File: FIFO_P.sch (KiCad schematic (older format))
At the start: 81 parts, among them J1 Vin, J2 ICLK, J3 Screw_Terminal_01x08, J4 Jack-DC, J5 Start Trigger, J6 Vout, SW1 Program History, SW2 Rotary_Encoder_61C, U1 IDT_ICS551, U10 AD7840, U11 LM2776, U2 SN74LVC2G157_MUX_TI, U3 SN74LVC2G157_MUX_TI, U4 LTC1740, U5 LM2940CT-5.0, U6 LM1117-3.3, U7 ARDUINO_DUE_FIFO_P_COMMANDS, U8 IDT_72V2105, U9 Adafruit_128x32_OLED_I2C_1306

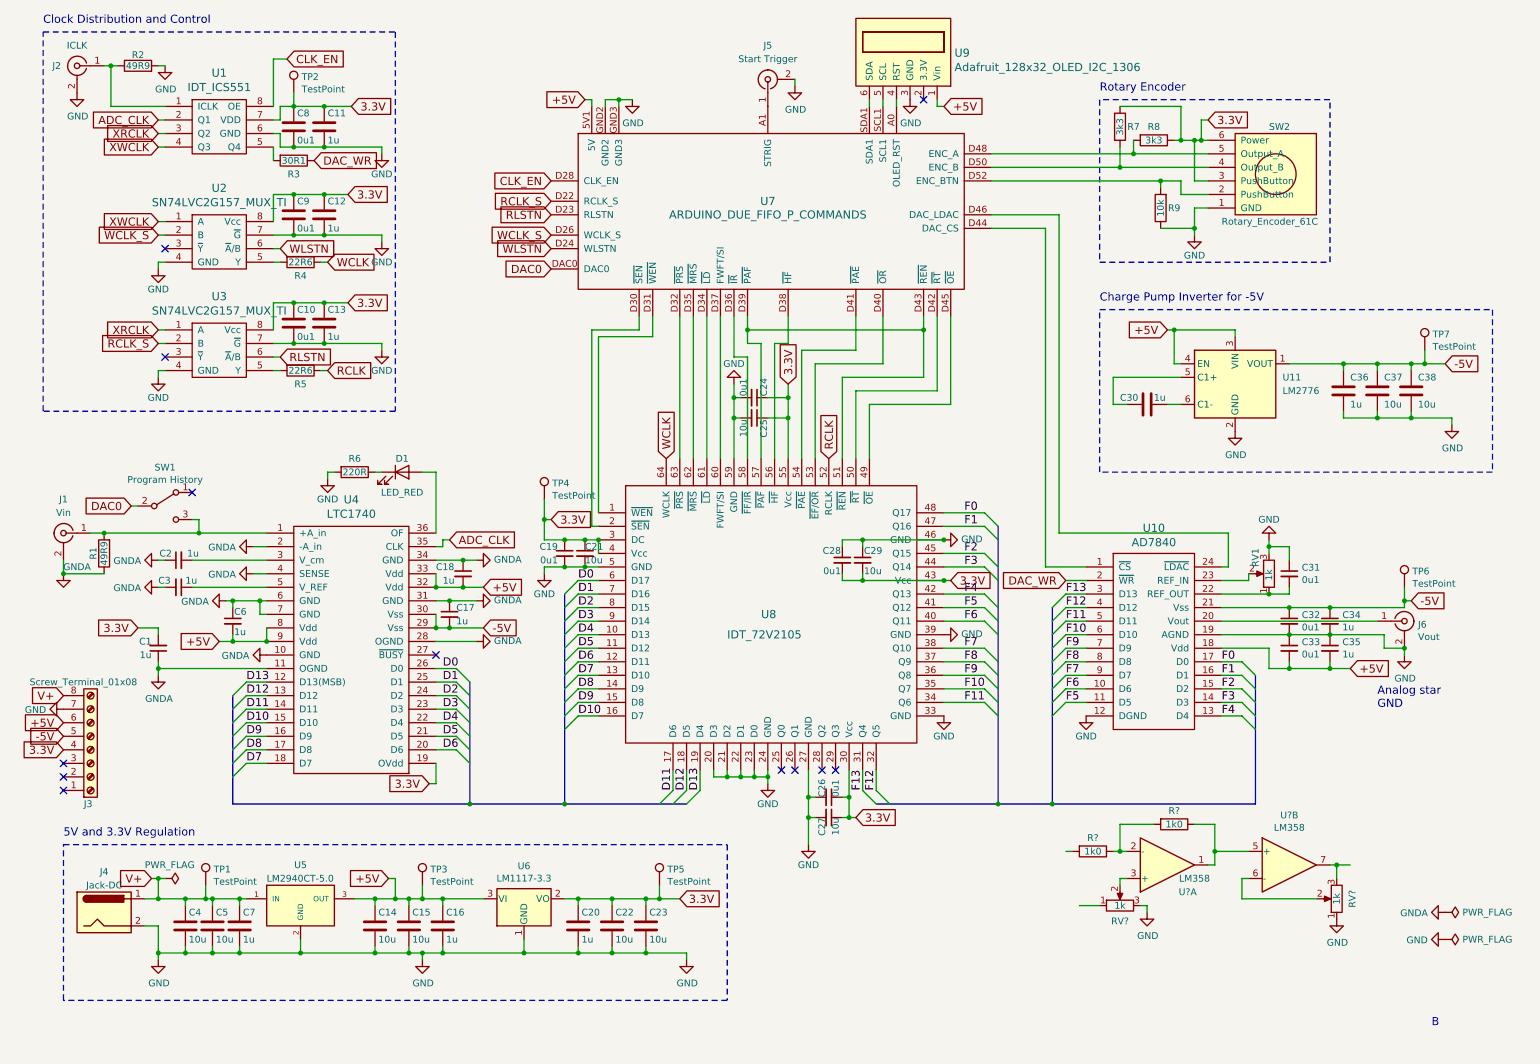
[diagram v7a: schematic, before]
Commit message: Finished DAC0 to ADC rescale circuit; rerouted power
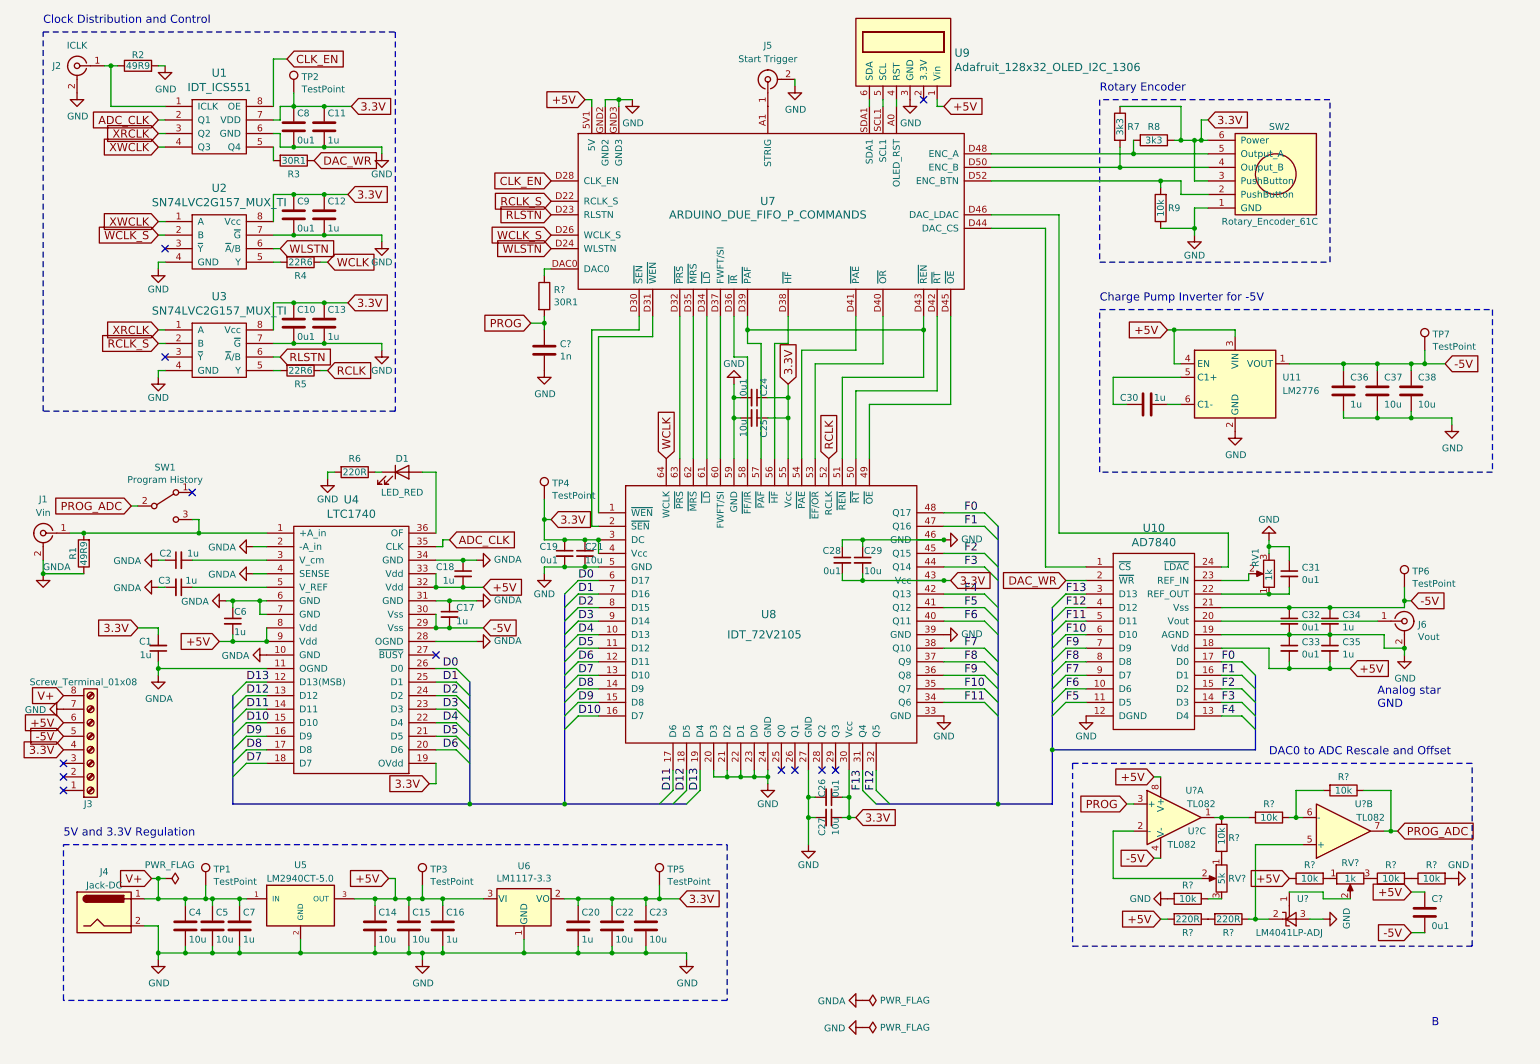
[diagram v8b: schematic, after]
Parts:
- removed RV? (x2): 1k, symbol Device:R_POT
- removed U? (x2): LM358, symbol Amplifier_Operational:LM358
- added C?: 0u1, symbol Device:C
- added C?: 1n, symbol Device:C
- added R? (x2): 220R, symbol Device:R
- added R?: 30R1, symbol Device:R
- added R? (x5): 10k, symbol Device:R
- added RV?: 1k, symbol Device:R_POT
- added RV?: 5k, symbol Device:R_POT
- added U? (x3): TL082, symbol Amplifier_Operational:TL082
- added U?: LM4041LP-ADJ, Package_TO_SOT_THT:TO-92_Inline, symbol Reference_Voltage:LM4041LP-ADJ
- R? (x2): value 1k0 -> 10k
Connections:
- net +5V: now also C?.1, R?.1, R?.2, U?.8 (V+)
- net -5V: now also C?.2, U?.4 (V-)
- net GND: now also C?.2, R?.2, R?.2, U?.3 (A)
- net PROG_ADC: now reaches R?.1
- net PROG_ADC: now also SW1.2 (B), U?.7
- net at R?.1, R?.2: now also U?.6 (-)
- net at R?.2: now also R?.1, U?.1
- net DAC0: no longer names the net of U7.DAC0
- net DAC0: now also R?.1; no longer SW1.2 (B)
- new net: R?.1, U?.2 (K), U?.5 (+)
- new net: R?.1, R?.2 (x2)
- new net: RV?.2, U?.2 (-)
- new net: RV?.2, U?.1 (FB)
- new net: R?.1, RV?.3 (x2)
- new net: R?.2, RV?.1 (x2)
- new net PROG: C?.1, R?.2, U?.3 (+)
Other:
- note added: "DAC0 to ADC Rescale and Offset"
- moved on the sheet: J1, R1, R?
